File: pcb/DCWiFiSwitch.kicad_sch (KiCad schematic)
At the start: 47 parts, among them J1 Screw_Terminal_01x06, J2 Conn_01x06, Q1 AO3400A, Q2 AO3400A, SW1 SW1_BOOT, U1 TPS5430DDA, U2 EL817, U3 EL817, U4 ESP-12F

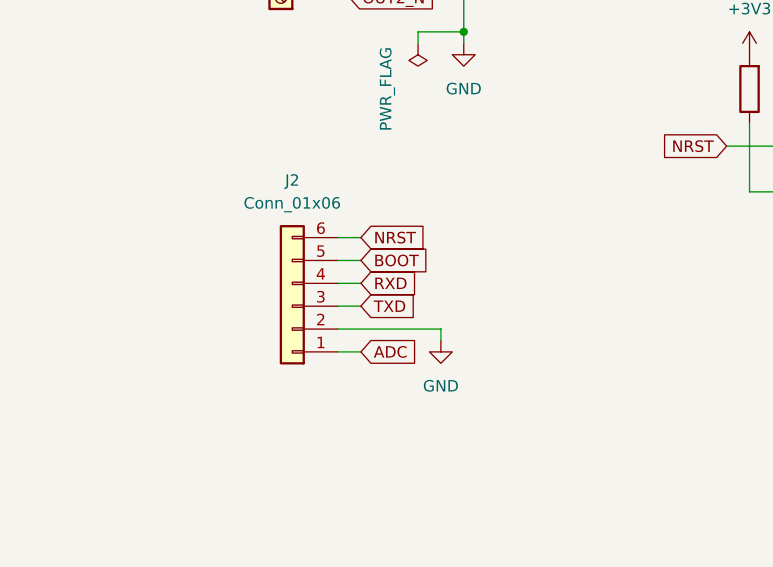
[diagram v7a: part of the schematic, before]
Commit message: add 3v3 to the pinheader, tweaked board
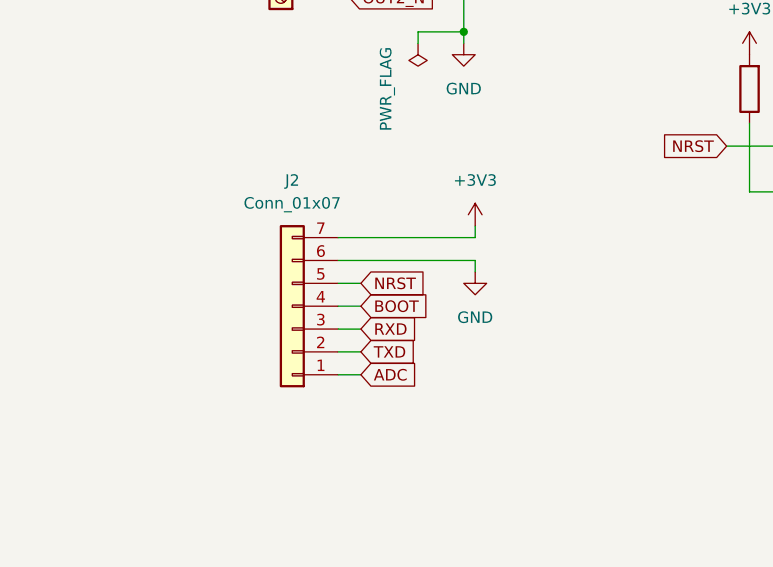
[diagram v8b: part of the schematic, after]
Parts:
- J2: value Conn_01x06 -> Conn_01x07; footprint Connector_PinHeader_2.54mm:PinHeader_1x06_P2.54mm_Vertical -> Connector_PinHeader_2.54mm:PinHeader_1x07_P2.54mm_Vertical; symbol Connector_Generic:Conn_01x06 -> Connector_Generic:Conn_01x07
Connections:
- net +3V3: now also J2.7 (Pin_7)
- net BOOT: now also J2.4 (Pin_4); no longer J2.5 (Pin_5)
- net GND: now also J2.6 (Pin_6); no longer J2.2 (Pin_2)
- net NRST: now also J2.5 (Pin_5); no longer J2.6 (Pin_6)
- net RXD: now also J2.3 (Pin_3); no longer J2.4 (Pin_4)
- net TXD: now also J2.2 (Pin_2); no longer J2.3 (Pin_3)
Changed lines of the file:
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@@
 	(wire
 		(pts
-			(xy 138.43 109.22) (xy 140.97 109.22)
+			(xy 67.31 119.38) (xy 67.31 118.11)
 		)
 		(stroke
@@
 	(wire
 		(pts
-			(xy 95.25 48.26) (xy 95.25 49.53)
+			(xy 138.43 109.22) (xy 140.97 109.22)
 		)
 		(stroke
@@
 	(wire
 		(pts
-			(xy 163.83 31.75) (xy 163.83 29.21)
+			(xy 95.25 48.26) (xy 95.25 49.53)
 		)
 		(stroke
@@
 	(wire
 		(pts
-			(xy 151.13 31.75) (xy 153.67 31.75)
+			(xy 163.83 31.75) (xy 163.83 29.21)
 		)
 		(stroke
@@
 	(wire
 		(pts
-			(xy 123.19 91.44) (xy 123.19 92.71)
+			(xy 151.13 31.75) (xy 153.67 31.75)
 		)
 		(stroke
@@
 	(wire
 		(pts
-			(xy 72.39 41.91) (xy 72.39 44.45)
+			(xy 123.19 91.44) (xy 123.19 92.71)
 		)
 		(stroke
@@
 	(wire
 		(pts
-			(xy 46.99 31.75) (xy 59.69 31.75)
+			(xy 72.39 41.91) (xy 72.39 44.45)
 		)
 		(stroke
@@
 	(wire
 		(pts
-			(xy 50.8 87.63) (xy 53.34 87.63)
+			(xy 46.99 31.75) (xy 59.69 31.75)
 		)
 		(stroke
@@
 	(wire
 		(pts
-			(xy 63.5 129.54) (xy 63.5 130.81)
+			(xy 50.8 87.63) (xy 53.34 87.63)
 		)
 		(stroke
@@
 	(wire
 		(pts
-			(xy 52.07 124.46) (xy 54.61 124.46)
+			(xy 52.07 129.54) (xy 54.61 129.54)
 		)
 		(stroke
@@
 	(wire
 		(pts
-			(xy 52.07 119.38) (xy 54.61 119.38)
+			(xy 52.07 124.46) (xy 54.61 124.46)
 		)
 		(stroke
@@
 	(wire
 		(pts
+			(xy 52.07 119.38) (xy 67.31 119.38)
+		)
+		(stroke
+			(width 0)
+			(type default)
+		)
+	)
+	(wire
+		(pts
 			(xy 41.91 31.75) (xy 46.99 31.75)
 		)
@@
 	(wire
 		(pts
-			(xy 52.07 132.08) (xy 54.61 132.08)
+			(xy 52.07 134.62) (xy 54.61 134.62)
 		)
 		(stroke
@@
 	(wire
 		(pts
-			(xy 52.07 129.54) (xy 63.5 129.54)
-		)
-		(stroke
-			(width 0)
-			(type default)
-		)
-	)
-	(wire
-		(pts
 			(xy 97.79 114.3) (xy 107.95 114.3)
 		)
@@
 	(wire
 		(pts
-			(xy 52.07 127) (xy 54.61 127)
+			(xy 52.07 132.08) (xy 54.61 132.08)
+		)
+		(stroke
+			(width 0)
+			(type default)
+		)
+	)
+	(wire
+		(pts
+			(xy 52.07 121.92) (xy 67.31 121.92)
 		)
 		(stroke
@@
 	(wire
 		(pts
-			(xy 52.07 121.92) (xy 54.61 121.92)
+			(xy 52.07 127) (xy 54.61 127)
 		)
 		(stroke
@@
 		)
 	)
+	(wire
+		(pts
+			(xy 67.31 121.92) (xy 67.31 123.19)
+		)
+		(stroke
+			(width 0)
+			(type default)
+		)
+	)
 	(global_label "NRST"
 		(shape input)
@@
 	(global_label "BOOT"
 		(shape input)
-		(at 54.61 121.92 0)
+		(at 54.61 127 0)
 		(fields_autoplaced yes)
 		(effects
@@
 		)
 		(property "Intersheetrefs" "${INTERSHEET_REFS}"
-			(at 62.4938 121.92 0)
+			(at 62.4938 127 0)
 			(effects
 				(font
@@
 	(global_label "TXD"
 		(shape input)
-		(at 54.61 127 0)
+		(at 54.61 132.08 0)
 		(fields_autoplaced yes)
 		(effects
@@
 		)
 		(property "Intersheetrefs" "${INTERSHEET_REFS}"
-			(at 61.0423 127 0)
+			(at 61.0423 132.08 0)
 			(effects
 				(font
@@
 	(global_label "NRST"
 		(shape input)
-		(at 54.61 119.38 0)
+		(at 54.61 124.46 0)
 		(fields_autoplaced yes)
 		(effects
@@
 		)
 		(property "Intersheetrefs" "${INTERSHEET_REFS}"
-			(at 62.3728 119.38 0)
+			(at 62.3728 124.46 0)
 			(effects
 				(font
@@
 	(global_label "ADC"
 		(shape input)
-		(at 54.61 132.08 0)
+		(at 54.61 134.62 0)
 		(fields_autoplaced yes)
 		(effects
@@
 		)
 		(property "Intersheetrefs" "${INTERSHEET_REFS}"
-			(at 61.2238 132.08 0)
+			(at 61.2238 134.62 0)
 			(effects
 				(font
@@
 	(global_label "RXD"
 		(shape input)
-		(at 54.61 124.46 0)
+		(at 54.61 129.54 0)
 		(fields_autoplaced yes)
 		(effects
@@
 		)
 		(property "Intersheetrefs" "${INTERSHEET_REFS}"
-			(at 61.3447 124.46 0)
+			(at 61.3447 129.54 0)
 			(effects
 				(font
@@
 	)
 	(symbol
+		(lib_id "power:+3V3")
+		(at 67.31 118.11 0)
+		(unit 1)
+		(exclude_from_sim no)
+		(in_bom yes)
+		(on_board yes)
+		(dnp no)
+		(fields_autoplaced yes)
+		(property "Reference" "#PWR028"
+			(at 67.31 121.92 0)
+			(effects
+				(font
+					(size 1.27 1.27)
+				)
+				(hide yes)
+			)
+		)
+		(property "Value" "+3V3"
+			(at 67.31 113.03 0)
+			(effects
+				(font
+					(size 1.27 1.27)
+				)
+			)
+		)
+		(property "Footprint" ""
+			(at 67.31 118.11 0)
+			(effects
+				(font
+					(size 1.27 1.27)
+				)
+				(hide yes)
+			)
+		)
+		(property "Datasheet" ""
+			(at 67.31 118.11 0)
+			(effects
+				(font
+					(size 1.27 1.27)
+				)
+				(hide yes)
+			)
+		)
+		(property "Description" "Power symbol creates a global label with name \"+3V3\""
+			(at 67.31 118.11 0)
+			(effects
+				(font
+					(size 1.27 1.27)
+				)
+				(hide yes)
+			)
+		)
+		(pin "1"
+		)
+		(instances
+			(project "DCWiFiSwitch"
+				(path "/2bcf36d7-c0ba-4c16-848a-400e98718055"
+					(reference "#PWR028")
+					(unit 1)
+				)
+			)
+		)
+	)
+	(symbol
 		(lib_id "Device:R")
 		(at 140.97 138.43 180)
@@
 	)
 	(symbol
-		(lib_id "Connector_Generic:Conn_01x06")
+		(lib_id "Connector_Generic:Conn_01x07")
 		(at 46.99 127 180)
 		(unit 1)
@@
 			)
 		)
-		(property "Value" "Conn_01x06"
+		(property "Value" "Conn_01x07"
 			(at 46.99 115.57 0)
 			(effects
@@
 			)
 		)
-		(property "Footprint" "Connector_PinHeader_2.54mm:PinHeader_1x06_P2.54mm_Vertical"
+		(property "Footprint" "Connector_PinHeader_2.54mm:PinHeader_1x07_P2.54mm_Vertical"
 			(at 46.99 127 0)
 			(effects
@@
 			)
 		)
-		(property "Description" "Generic connector, single row, 01x06, script generated (kicad-library-utils/schlib/autogen/connector/)"
+		(property "Description" "Generic connector, single row, 01x07, script generated (kicad-library-utils/schlib/autogen/connector/)"
 			(at 46.99 127 0)
 			(effects
@@
 		(pin "2"
 		)
+		(pin "7"
+		)
 		(instances
 			(project ""
@@
 	(symbol
 		(lib_id "power:GND")
-		(at 63.5 130.81 0)
+		(at 67.31 123.19 0)
 		(unit 1)
 		(exclude_from_sim no)
@@
 		(fields_autoplaced yes)
 		(property "Reference" "#PWR020"
-			(at 63.5 137.16 0)
+			(at 67.31 129.54 0)
 			(effects
 				(font
@@
 		)
 		(property "Value" "GND"
-			(at 63.5 135.89 0)
+			(at 67.31 128.27 0)
 			(effects
 				(font
@@
 		)
 		(property "Footprint" ""
-			(at 63.5 130.81 0)
+			(at 67.31 123.19 0)
 			(effects
 				(font
@@
 		)
 		(property "Datasheet" ""
-			(at 63.5 130.81 0)
+			(at 67.31 123.19 0)
 			(effects
 				(font
@@
 		)
 		(property "Description" "Power symbol creates a global label with name \"GND\" , ground"
-			(at 63.5 130.81 0)
+			(at 67.31 123.19 0)
 			(effects
 				(font
